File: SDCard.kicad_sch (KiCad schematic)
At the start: 5 parts, among them J12 Micro_SD_Card_Det, U19 RT9742GGJ5

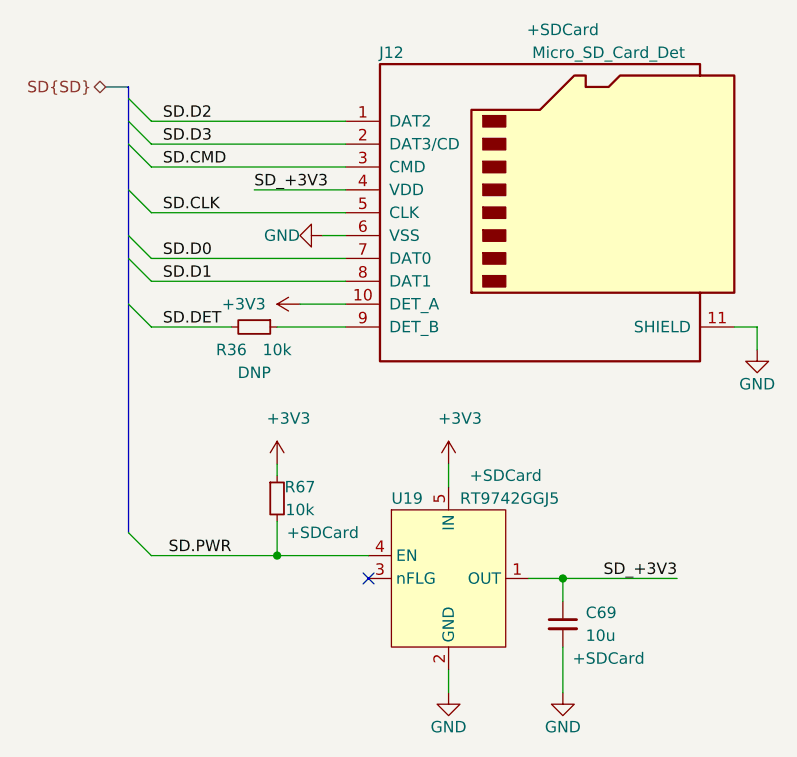
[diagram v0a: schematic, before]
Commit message: Reannotate the complete schematics
Signed-off-by: Stefan Agner <stefan@agner.ch>
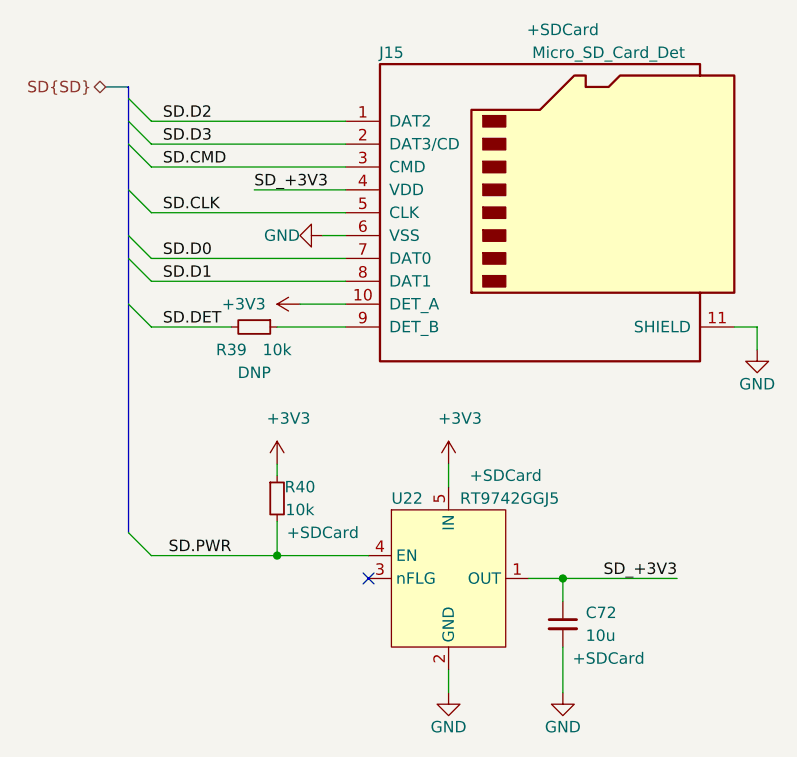
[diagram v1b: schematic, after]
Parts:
- renumbered C69 to C72, J12 to J15, R36 to R39, R67 to R40, U19 to U22
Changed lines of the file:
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@@
   (symbol (lib_id "power:+3V3") (at 72.39 99.06 0) (unit 1)
     (in_bom yes) (on_board yes)
-    (property "Reference" "#PWR0288" (id 0) (at 72.39 102.87 0)
+    (property "Reference" "#PWR0147" (id 0) (at 72.39 102.87 0)
       (effects (font (size 1.27 1.27)) hide)
     )
@@
   (symbol (lib_id "power:+3V3") (at 74.93 81.28 90) (unit 1)
     (in_bom yes) (on_board yes)
-    (property "Reference" "#PWR0243" (id 0) (at 78.74 81.28 0)
+    (property "Reference" "#PWR0148" (id 0) (at 78.74 81.28 0)
       (effects (font (size 1.27 1.27)) hide)
     )
@@
   (symbol (lib_id "power:+3V3") (at 91.44 99.06 0) (unit 1)
     (in_bom yes) (on_board yes)
-    (property "Reference" "#PWR0239" (id 0) (at 91.44 102.87 0)
+    (property "Reference" "#PWR0150" (id 0) (at 91.44 102.87 0)
       (effects (font (size 1.27 1.27)) hide)
     )
@@
   (symbol (lib_id "power:GND") (at 77.47 73.66 270) (unit 1)
     (in_bom yes) (on_board yes)
-    (property "Reference" "#PWR0238" (id 0) (at 71.12 73.66 0)
+    (property "Reference" "#PWR0149" (id 0) (at 71.12 73.66 0)
       (effects (font (size 1.27 1.27)) hide)
     )
@@
   (symbol (lib_id "power:GND") (at 91.44 124.46 0) (unit 1)
     (in_bom yes) (on_board yes)
-    (property "Reference" "#PWR0242" (id 0) (at 91.44 130.81 0)
+    (property "Reference" "#PWR0151" (id 0) (at 91.44 130.81 0)
       (effects (font (size 1.27 1.27)) hide)
     )
@@
   (symbol (lib_id "power:GND") (at 104.14 124.46 0) (unit 1)
     (in_bom yes) (on_board yes)
-    (property "Reference" "#PWR0241" (id 0) (at 104.14 130.81 0)
+    (property "Reference" "#PWR0152" (id 0) (at 104.14 130.81 0)
       (effects (font (size 1.27 1.27)) hide)
     )
@@
   (symbol (lib_id "power:GND") (at 125.73 86.36 0) (unit 1)
     (in_bom yes) (on_board yes)
-    (property "Reference" "#PWR0240" (id 0) (at 125.73 92.71 0)
+    (property "Reference" "#PWR0153" (id 0) (at 125.73 92.71 0)
       (effects (font (size 1.27 1.27)) hide)
     )
@@
   (symbol (lib_id "Device:R_Small") (at 69.85 83.82 270) (unit 1)
     (in_bom yes) (on_board yes)
-    (property "Reference" "R36" (id 0) (at 67.31 86.36 90))
+    (property "Reference" "R39" (id 0) (at 67.31 86.36 90))
     (property "Value" "10k" (id 1) (at 72.39 86.36 90))
     (property "Footprint" "Resistor_SMD:R_0402_1005Metric" (id 2) (at 69.85 83.82 0)
@@
   (symbol (lib_id "Device:R_Small") (at 72.39 102.87 0) (unit 1)
     (in_bom yes) (on_board yes)
-    (property "Reference" "R67" (id 0) (at 74.93 101.6 0))
+    (property "Reference" "R40" (id 0) (at 74.93 101.6 0))
     (property "Value" "10k" (id 1) (at 74.93 104.14 0))
     (property "Footprint" "Resistor_SMD:R_0402_1005Metric" (id 2) (at 72.39 102.87 0)
@@
   (symbol (lib_id "Device:C_Small") (at 104.14 116.84 0) (unit 1)
     (in_bom yes) (on_board yes)
-    (property "Reference" "C69" (id 0) (at 106.68 115.57 0)
+    (property "Reference" "C72" (id 0) (at 106.68 115.57 0)
       (effects (font (size 1.27 1.27)) (justify left))
     )
@@
   (symbol (lib_id "LightBlue:RT9742GGJ5") (at 91.44 111.76 0) (unit 1)
     (in_bom yes) (on_board yes)
-    (property "Reference" "U19" (id 0) (at 85.09 102.87 0)
+    (property "Reference" "U22" (id 0) (at 85.09 102.87 0)
       (effects (font (size 1.27 1.27)) (justify left))
     )
@@
   (symbol (lib_id "Connector:Micro_SD_Card_Det") (at 102.87 71.12 0) (unit 1)
     (in_bom yes) (on_board yes)
-    (property "Reference" "J12" (id 0) (at 85.09 53.34 0))
+    (property "Reference" "J15" (id 0) (at 85.09 53.34 0))
     (property "Value" "Micro_SD_Card_Det" (id 1) (at 109.22 53.34 0))
     (property "Footprint" "Connector_Card:microSD_HC_Molex_104031-0811" (id 2) (at 154.94 53.34 0)

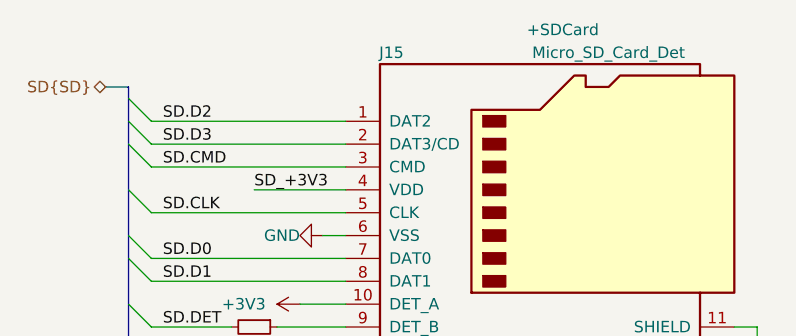
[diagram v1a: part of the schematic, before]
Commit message: Update silkscreen/adjust reference designators
Order some relevant reference designator. Use JP for all jumpers. Place
silkcreen neatly. Add some custom silk screen. Remove heat sink corner
marks on silk screen.

Signed-off-by: Stefan Agner <stefan@agner.ch>
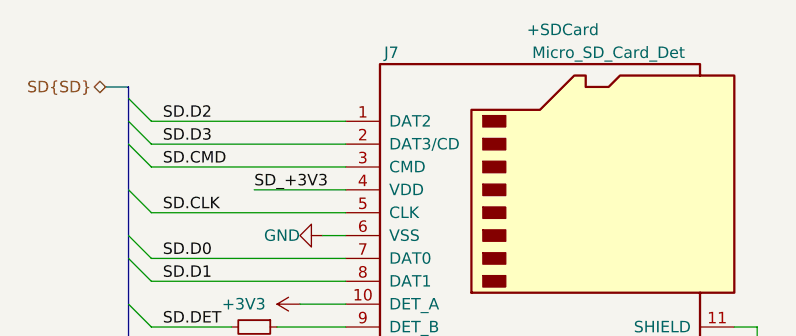
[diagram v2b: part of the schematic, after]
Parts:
- renumbered J15 to J7
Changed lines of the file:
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@@
   (symbol (lib_id "Connector:Micro_SD_Card_Det") (at 102.87 71.12 0) (unit 1)
     (in_bom yes) (on_board yes)
-    (property "Reference" "J15" (id 0) (at 85.09 53.34 0))
+    (property "Reference" "J7" (id 0) (at 85.09 53.34 0))
     (property "Value" "Micro_SD_Card_Det" (id 1) (at 109.22 53.34 0))
     (property "Footprint" "Connector_Card:microSD_HC_Molex_104031-0811" (id 2) (at 154.94 53.34 0)

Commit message: Renmae LightBlue to Amber
Signed-off-by: Stefan Agner <stefan@agner.ch>
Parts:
- U22: symbol LightBlue:RT9742GGJ5 -> Amber:RT9742GGJ5
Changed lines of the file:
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@@
     (company "Nabu Casa")
     (comment 1 "www.nabucasa.com")
-    (comment 2 "Light Blue")
+    (comment 2 "Amber")
   )
   (junction (at 72.39 109.22) (diameter 0.9144) (color 0 0 0 0))
@@
     (pin "2")
   )
-  (symbol (lib_id "LightBlue:RT9742GGJ5") (at 91.44 111.76 0) (unit 1)
+  (symbol (lib_id "Amber:RT9742GGJ5") (at 91.44 111.76 0) (unit 1)
     (in_bom yes) (on_board yes)
     (property "Reference" "U22" (id 0) (at 85.09 102.87 0)
